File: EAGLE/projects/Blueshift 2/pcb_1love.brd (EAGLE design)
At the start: 96.5 x 226.1 mm, 20 parts, among them X1 RASPI_BOARD_B+_F

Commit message: Re-position components
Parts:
- moved PWM_EXT 110.6 mm to (89.5, 218.4), flipped to the bottom, turned to 270 degrees
- moved U$1 64.1 mm to (55.9, 135.3), turned to 90 degrees
- moved X1 59.7 mm to (59.1, 136.5), turned to 90 degrees
- moved IMU 43.9 mm to (62.9, 191.1)
- moved VCONVERTER 17.3 mm to (74.9, 142.9)
- moved CONN14 13.4 mm to (88.9, 151.8)
- moved TP_ESC_F 1.27 mm to (90.2, 130.8)
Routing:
- net N$2: track 198.1 -> 0.00 mm
- net N$1: track 191.5 -> 0.00 mm
- net +24V: track 120.9 -> 0.00 mm
- net +18V: track 116.6 -> 0.00 mm
- net N$4: track 101.6 -> 0.00 mm
- net N$3: track 18.9 -> 0.00 mm
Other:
- outline, holes or cut-outs redrawn

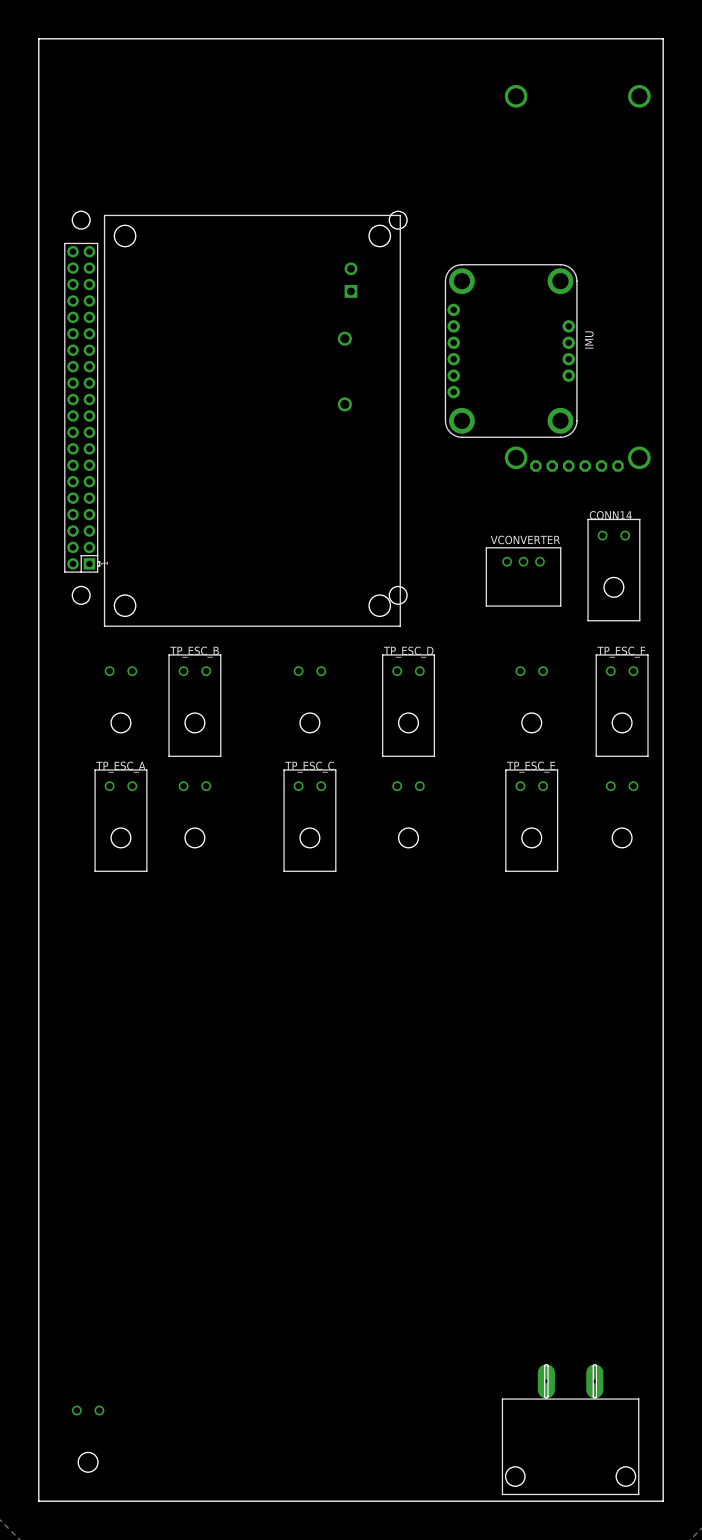
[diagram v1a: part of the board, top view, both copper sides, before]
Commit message: Add wires and cutout for new layout
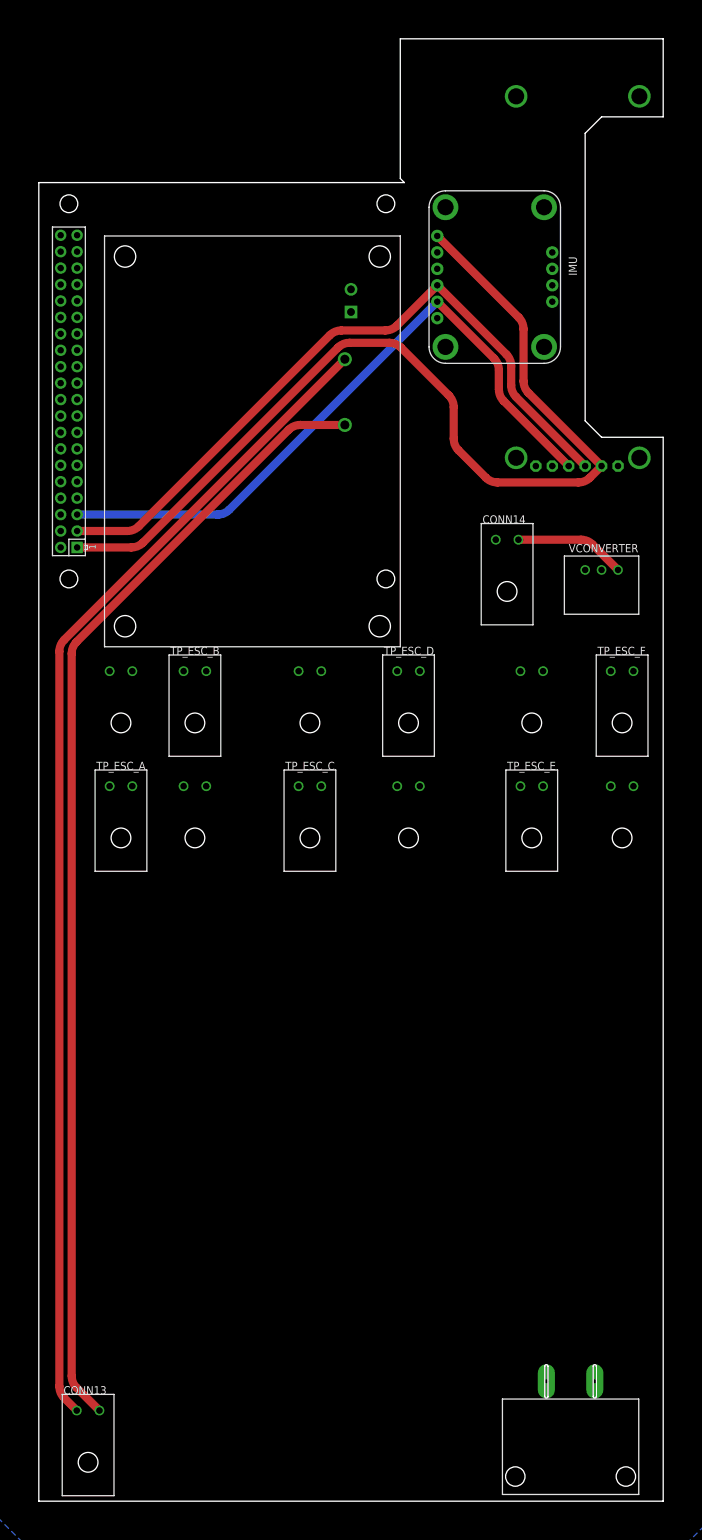
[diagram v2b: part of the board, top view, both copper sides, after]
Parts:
- moved CONN14 16.5 mm to (72.4, 151.1)
- moved VCONVERTER 12.1 mm to (87.0, 141.6)
- moved IMU 11.7 mm to (60.3, 202.6)
- moved X1 3.17 mm to (57.1, 139.1)
- moved U$1 3.17 mm to (55.9, 132.1)
- flipped CONN13 to the top
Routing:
- net N$2: track 0.00 -> 181.6 mm
- net N$1: track 0.00 -> 175.8 mm
- net N$4: track 0.00 -> 152.9 mm
- net +18V: track 0.00 -> 108.0 mm
- net +24V: track 0.00 -> 102.6 mm
- net N$3: track 0.00 -> 17.2 mm
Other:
- outline, holes or cut-outs redrawn
